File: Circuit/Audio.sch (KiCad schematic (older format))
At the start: 12 parts, among them U5 NAU8814

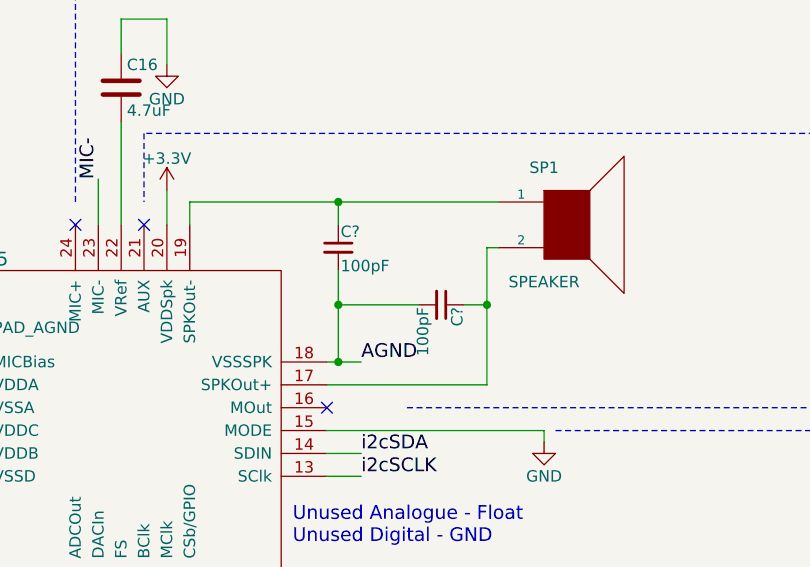
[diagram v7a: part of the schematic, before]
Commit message: Updated Alligator tabs
Incomplete.  Included to provide ideas.
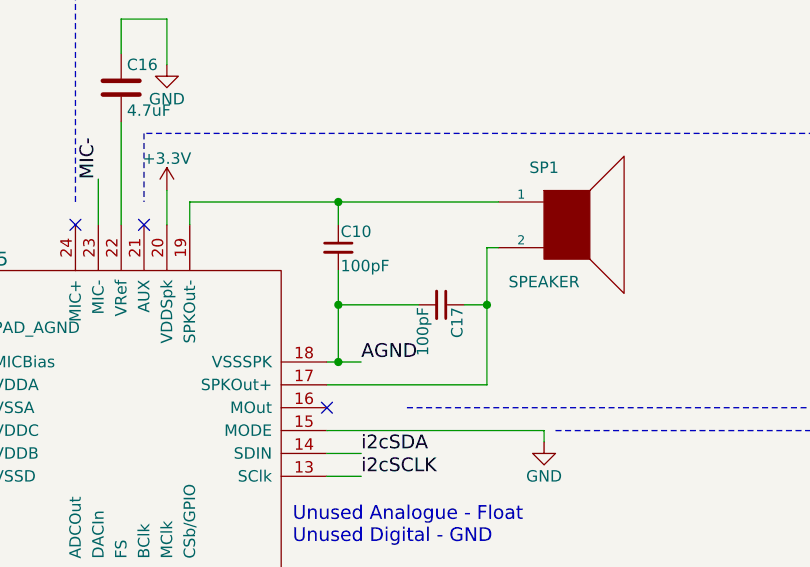
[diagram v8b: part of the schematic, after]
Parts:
- gave numbers to parts that had none: 2
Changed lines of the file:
@@
 	1400 3900 1550 3900
 $Comp
-L C_Small C?
+L C_Small C17
 U 1 1 581FF4BD
 P 6950 3250
-F 0 "C?" H 6960 3320 50  0000 L CNN
+F 0 "C17" H 6960 3320 50  0000 L CNN
 F 1 "100pF" H 6960 3170 50  0000 L CNN
 F 2 "Capacitors_SMD:C_0603_HandSoldering" H 6950 3250 50  0001 C CNN
@@
 $EndComp
 $Comp
-L C_Small C?
+L C_Small C10
 U 1 1 5820032A
 P 6500 3000
-F 0 "C?" H 6510 3070 50  0000 L CNN
+F 0 "C10" H 6510 3070 50  0000 L CNN
 F 1 "100pF" H 6510 2920 50  0000 L CNN
 F 2 "Capacitors_SMD:C_0603_HandSoldering" H 6500 3000 50  0001 C CNN
